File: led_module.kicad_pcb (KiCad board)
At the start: 2 copper layers, 52.1 x 29.2 mm, 3 parts, among them J1 Conn_02x20_Odd_Even

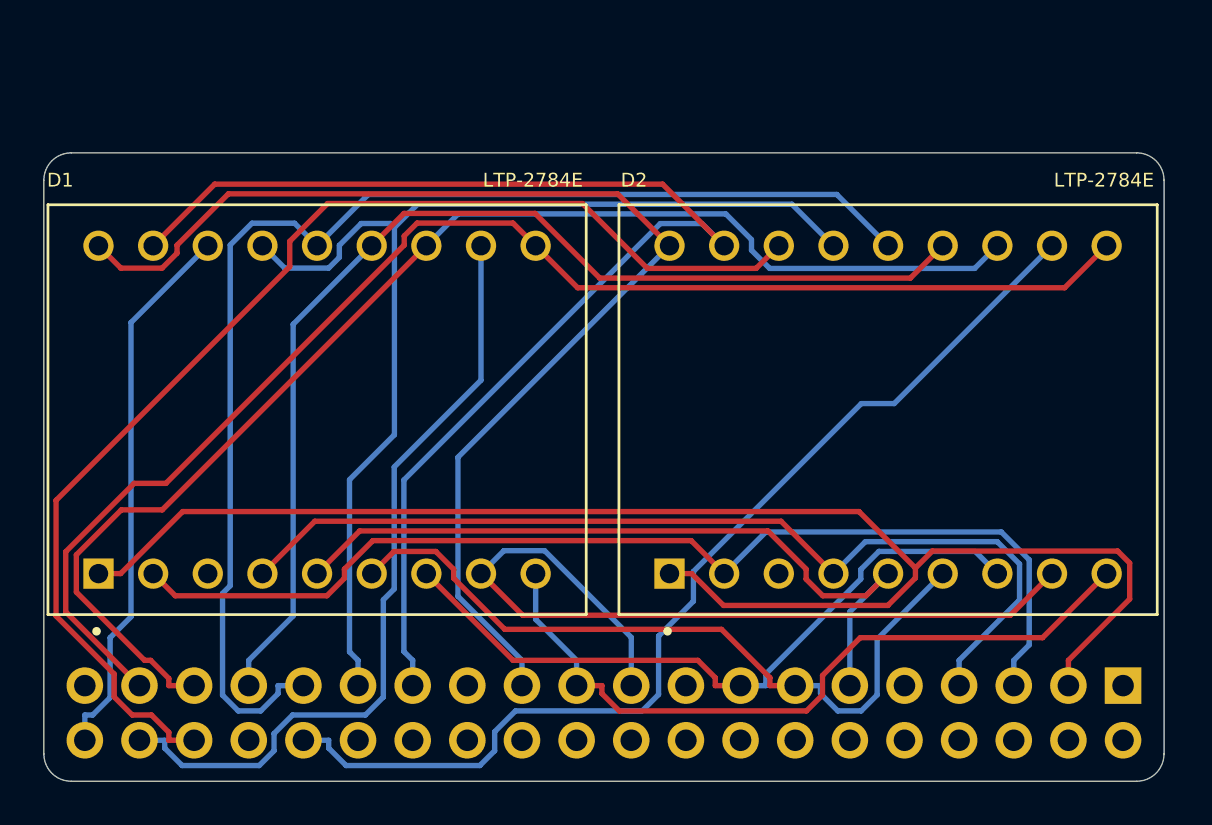
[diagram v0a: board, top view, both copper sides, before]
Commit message: Rev B.  Improve brightness by using 2N7000 MOSFETs to switch digits.  Use only RPi pins that are not shared with PMOD-A.
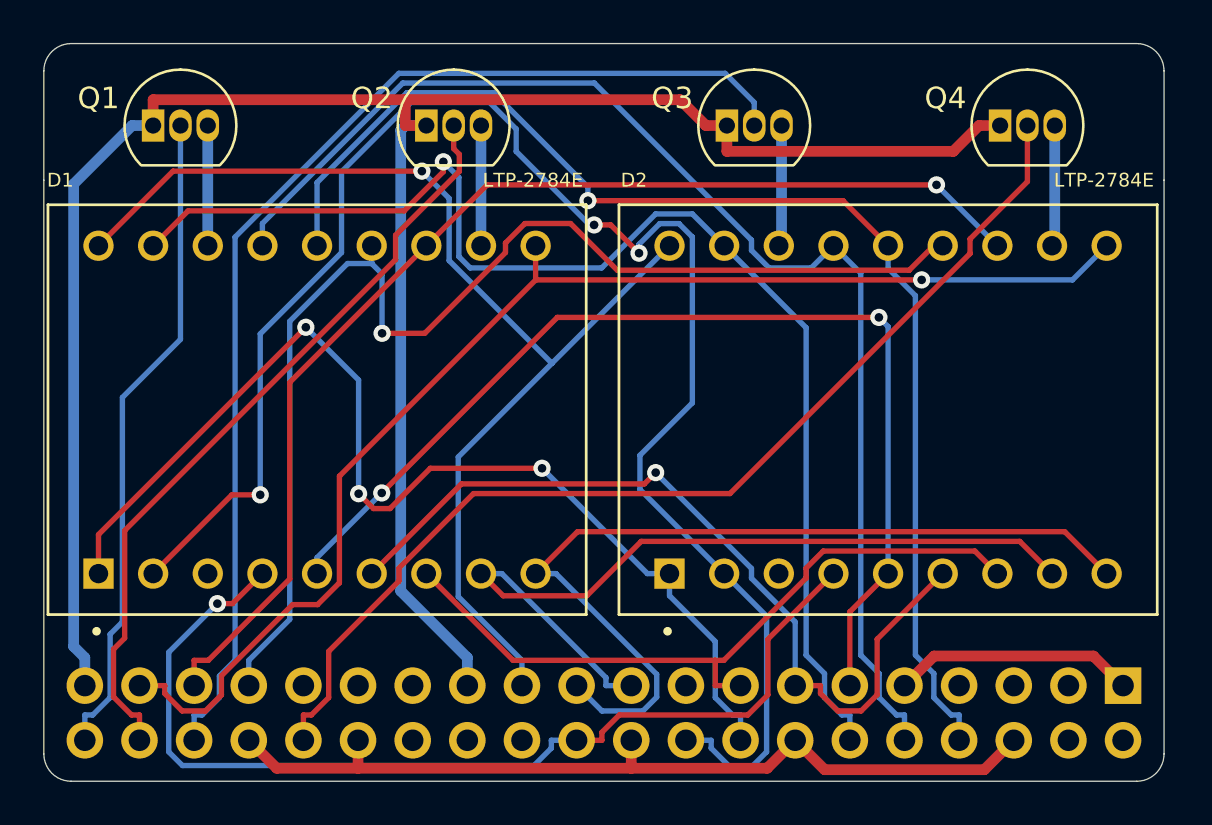
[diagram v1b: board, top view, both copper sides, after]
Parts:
- added Q1: 2N7000, Package_TO_SOT_THT:TO-92_Inline, F.Cu at (33.0, 100.3)
- added Q2: 2N7000, Package_TO_SOT_THT:TO-92_Inline, F.Cu at (45.7, 100.3)
- added Q3: 2N7000, Package_TO_SOT_THT:TO-92_Inline, F.Cu at (59.7, 100.3)
- added Q4: 2N7000, Package_TO_SOT_THT:TO-92_Inline, F.Cu at (72.4, 100.3)
- added REF**: OSHW-Logo2_9.8x8mm_SilkScreen, Symbol:OSHW-Logo2_9.8x8mm_SilkScreen, B.Cu at (53.3, 114.3)
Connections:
- J1 pad 1: (no net) -> GND
- J1 pad 10: (no net) -> Net-(D1-Pad15)
- J1 pad 12: (no net) -> Net-(D1-Pad17)
- J1 pad 14: (no net) -> GND
- J1 pad 16: (no net) -> Net-(D1-Pad1)
- J1 pad 18: (no net) -> Net-(D1-Pad2)
- J1 pad 20: (no net) -> GND
- J1 pad 22: (no net) -> Net-(D1-Pad4)
- J1 pad 25: (no net) -> GND
- J1 pad 27: Net-(D1-Pad17) -> (no net)
- J1 pad 29: Net-(D1-Pad15) -> (no net)
- J1 pad 3: Net-(D1-Pad1) -> (no net)
- J1 pad 30: (no net) -> GND
- J1 pad 31: Net-(D1-Pad14) -> (no net)
- J1 pad 32: Net-(D2-Pad11) -> Net-(J1-Pad32)
- J1 pad 34: (no net) -> GND
- J1 pad 36: Net-(D2-Pad16) -> Net-(J1-Pad36)
- J1 pad 38: Net-(D1-Pad11) -> Net-(J1-Pad38)
- J1 pad 39: (no net) -> GND
- J1 pad 40: Net-(D1-Pad16) -> Net-(J1-Pad40)
- J1 pad 5: Net-(D1-Pad2) -> (no net)
- J1 pad 6: (no net) -> GND
- J1 pad 7: Net-(D1-Pad4) -> (no net)
- J1 pad 8: (no net) -> Net-(D1-Pad14)
- J1 pad 9: (no net) -> GND
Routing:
- net GND: track 0.00 -> 153.3 mm
- net Net-(J1-Pad36): track 0.00 -> 53.3 mm
- net Net-(D2-Pad16): track 56.7 -> 5.64 mm
- net Net-(J1-Pad32): track 0.00 -> 49.7 mm
- net Net-(D2-Pad11): track 48.4 -> 5.64 mm
- net Net-(J1-Pad38): track 0.00 -> 36.1 mm
- net Net-(D1-Pad11): track 36.7 -> 5.59 mm
- net Net-(J1-Pad40): track 0.00 -> 30.6 mm
- net Net-(D1-Pad2): track 50.6 -> 77.4 mm, vias 0 -> 3
- net Net-(D1-Pad16): track 25.6 -> 5.59 mm
- net Net-(D1-Pad1): track 70.7 -> 51.1 mm, vias 0 -> 3
- net Net-(D1-Pad5): track 35.3 -> 49.5 mm, vias 0 -> 2
- net Net-(D1-Pad15): track 51.8 -> 59.1 mm
- net Net-(D1-Pad9): track 34.5 -> 41.3 mm
- net Net-(D1-Pad12): track 60.4 -> 54.2 mm, vias 0 -> 1
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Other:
- board size 52.1 x 29.2 mm -> 52.1 x 34.3 mm
- net class GND added: clearance 0.2, trace_width 0.5, via_dia 0.8, via_drill 0.4
